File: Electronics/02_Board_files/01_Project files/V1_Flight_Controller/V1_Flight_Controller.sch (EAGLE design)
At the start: 3 parts, among them U1 STM32F030K6T6, U2 MPU-6050

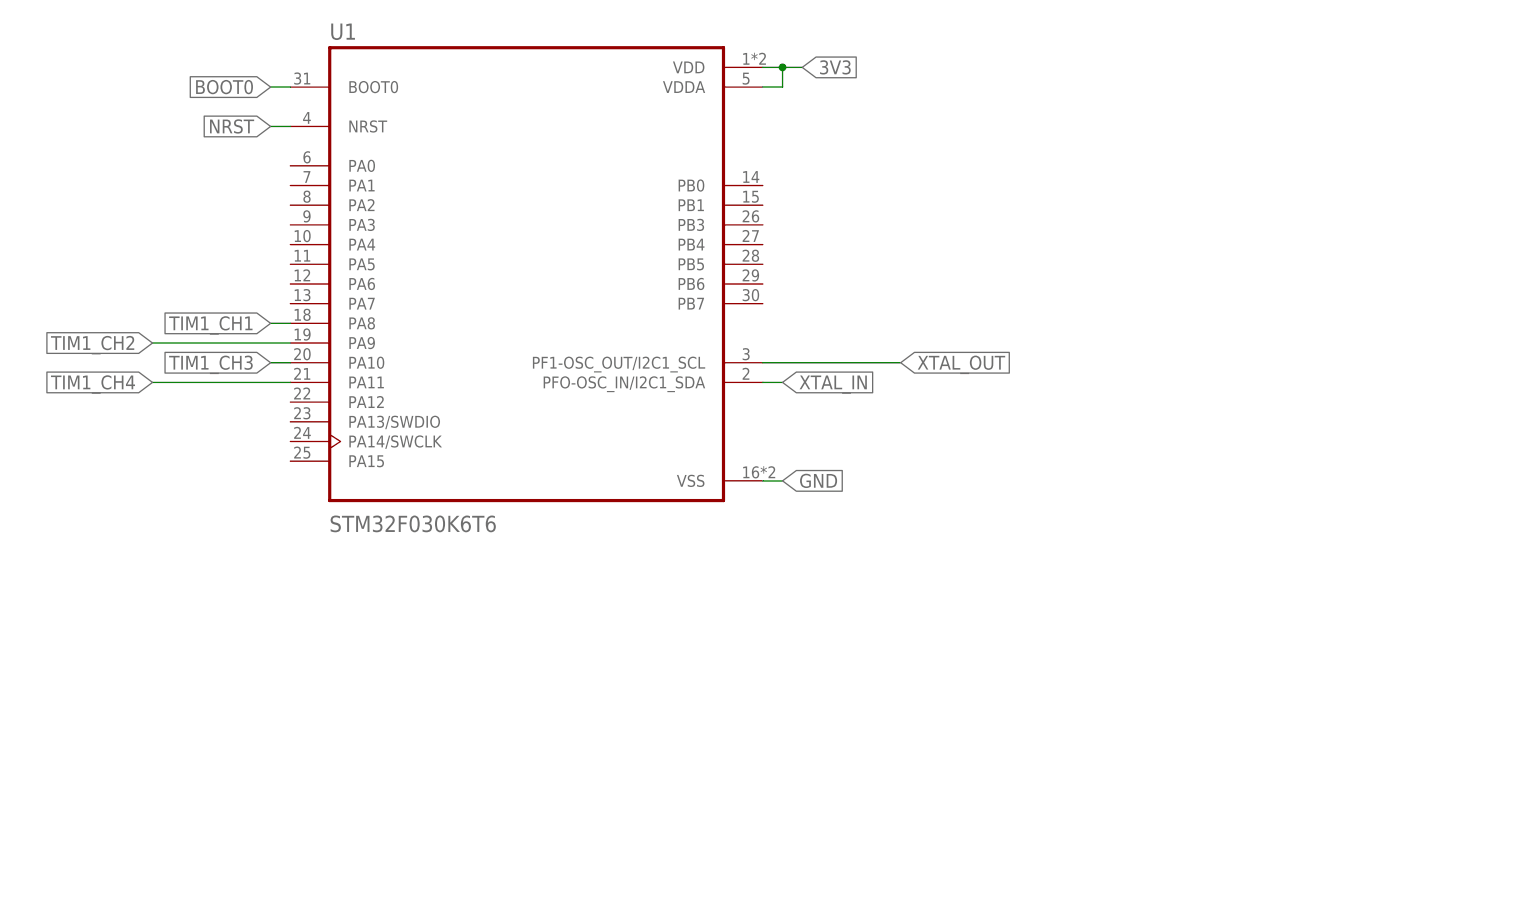
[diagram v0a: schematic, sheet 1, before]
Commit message: Schematic changes
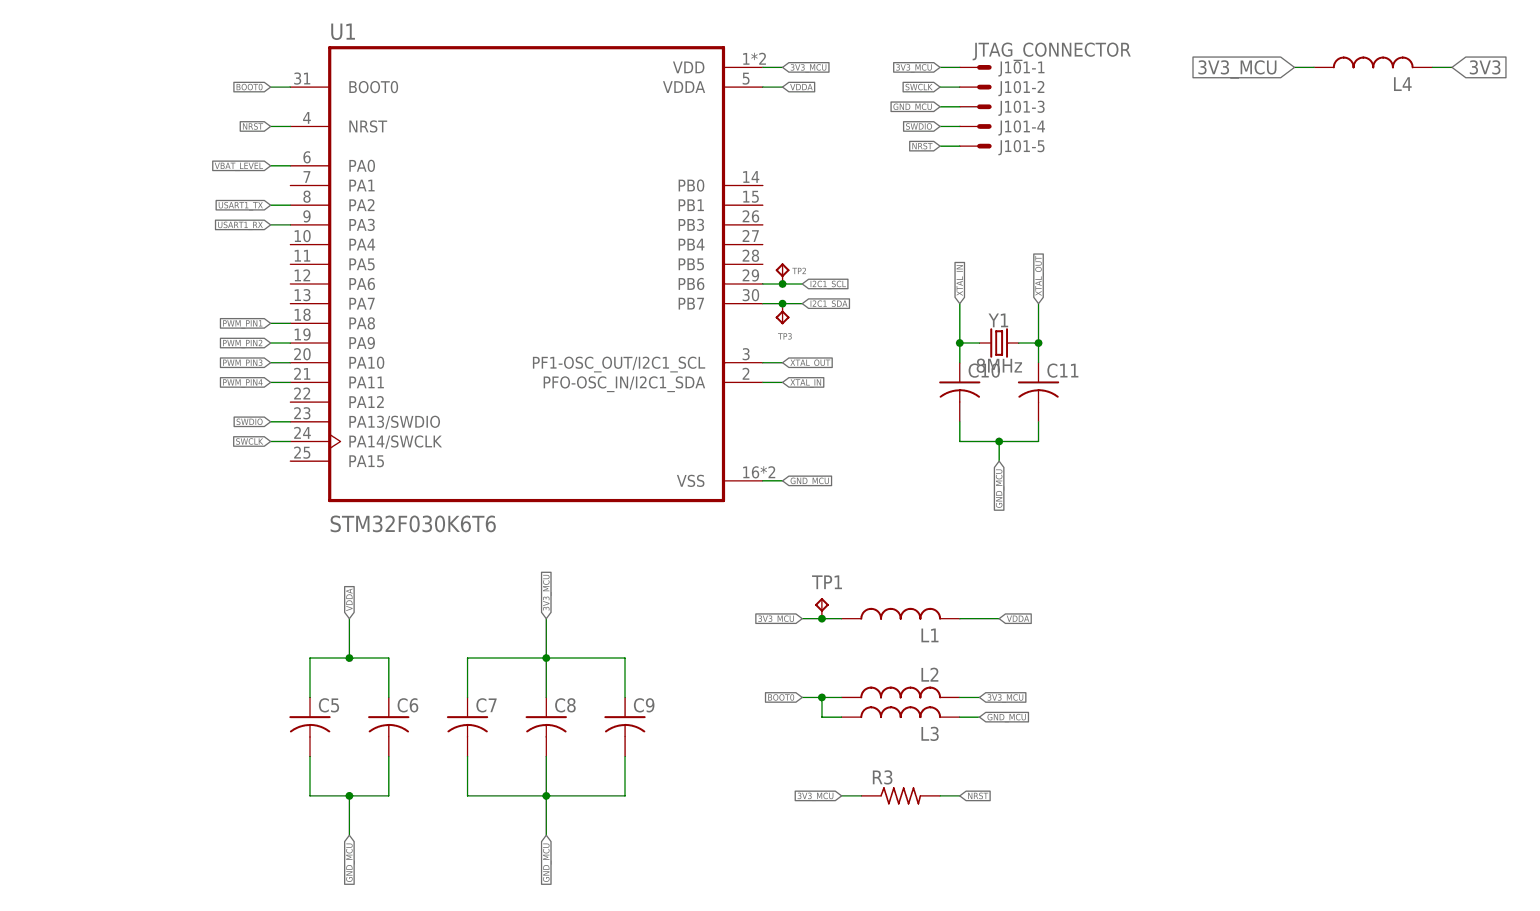
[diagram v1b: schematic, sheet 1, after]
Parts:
- added C1: 0.1uF, 2V, ±10%, adafruit:C-USC0603
- added C10, C11, C5, C6, C7, C8, C9: (no value), adafruit:C-USC0603
- added C2: 0.1uF, 4V, ±10%, adafruit:C-USC0603
- added C3: 2.2nF, 50V, ±10%, adafruit:C-USC0603
- added C4: 10nF, 4V, ±10%, adafruit:C-USC0603
- added J101: JTAG_CONNECTOR, con-molex:53047-05
- added L1, L2, L3, L4, L5: (no value), rcl:L-USL2012C
- added R1, R2: 4.7k, adafruit:R-US_R0603
- added R3: (no value), adafruit:R-US_R0603
- added TP1, TP2, TP3: TPB1,27, testpad:TPB1,27
- added Y1: 8MHz, SparkFun-Clocks:CRYSTAL-8MHZSMD-HC49UP
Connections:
- net TIM1_CH1 renamed PWM_PIN1
- net TIM1_CH2 renamed PWM_PIN2
- net TIM1_CH3 renamed PWM_PIN3
- net TIM1_CH4 renamed PWM_PIN4
- new net 3V3_IMU: C2.1, C4.1, L5.1, R1.1, R2.1, U2.VDD, U2.VLOGIC
- new net 3V3_MCU: C7.1, C8.1, C9.1, J101-1.S, L1.1, L2.2, L4.1, R3.1, TP1.TP, U1.VDD
- new net GND_IMU: C1.2, C2.2, C3.2, C4.2, U2.AD0, U2.CLKIN, U2.FSYNC, U2.GND
- new net GND_MCU: C10.2, C11.2, C5.2, C6.2, C7.2, C8.2, C9.2, J101-3.S, L3.2, U1.VSS
- new net I2C1_SCL: TP2.TP, U1.PB6
- new net I2C1_SDA: TP3.TP, U1.PB7
- new net IMU_INT: U2.INT
- new net N$1: C1.1, U2.REGOUT
- new net N$2: C3.1, U2.CPOUT
- new net SWCLK: J101-2.S, U1.PA14/SWCLK
- new net SWDIO: J101-4.S, U1.PA13/SWDIO
- new net USART1_RX: U1.PA3
- new net USART1_TX: U1.PA2
- new net VBAT_LEVEL: U1.PA0
- new net VDDA: C5.1, C6.1, L1.2, U1.VDDA
- net 3V3: now also L4.2, L5.2; no longer U1.VDD, U1.VDDA, U2.VDD, U2.VLOGIC
- net BOOT0: now also L2.1, L3.1
- net GND: no longer U1.VSS, U2.GND
- net NRST: now also J101-5.S, R3.2
- net SCL: now also R1.2
- net SDA: now also R2.2
- net XTAL_IN: now also C10.1, Y1.1
- net XTAL_OUT: now also C11.1, Y1.2

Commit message: added sheets for power section and motor driver
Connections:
- new net RST: SJR1.REST
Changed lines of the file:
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@@
 <instances>
 <instance part="SJR1" gate="G$1" x="5.08" y="2.54" smashed="yes">
-<attribute name="NAME" x="-5.08" y="15.24" size="1.27" layer="94"/>
+<attribute name="NAME" x="-5.08" y="15.24" size="1.27" layer="94" font="vector"/>
 </instance>
 </instances>
@@
 </segment>
 </net>
+<net name="RST" class="0">
+<segment>
+<pinref part="SJR1" gate="G$1" pin="REST"/>
+<wire x1="-17.78" y1="10.16" x2="-20.32" y2="10.16" width="0.1524" layer="91"/>
+<label x="-20.32" y="10.16" size="0.8128" layer="95" font="vector" rot="R180" xref="yes"/>
+</segment>
+</net>
 </nets>
 </sheet>
+<sheet>
+<description>Power Section</description>
+<plain>
+</plain>
+<instances>
+</instances>
+<busses>
+</busses>
+<nets>
+</nets>
+</sheet>
+<sheet>
+<description>Motor Driver</description>
+<plain>
+</plain>
+<instances>
+</instances>
+<busses>
+</busses>
+<nets>
+</nets>
+</sheet>
